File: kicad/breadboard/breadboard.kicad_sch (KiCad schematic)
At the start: 11 parts, among them U1 74LS245, U2 74LS245, U3 UPdruino_v3.0, U4 74LS245, U5 74LS245

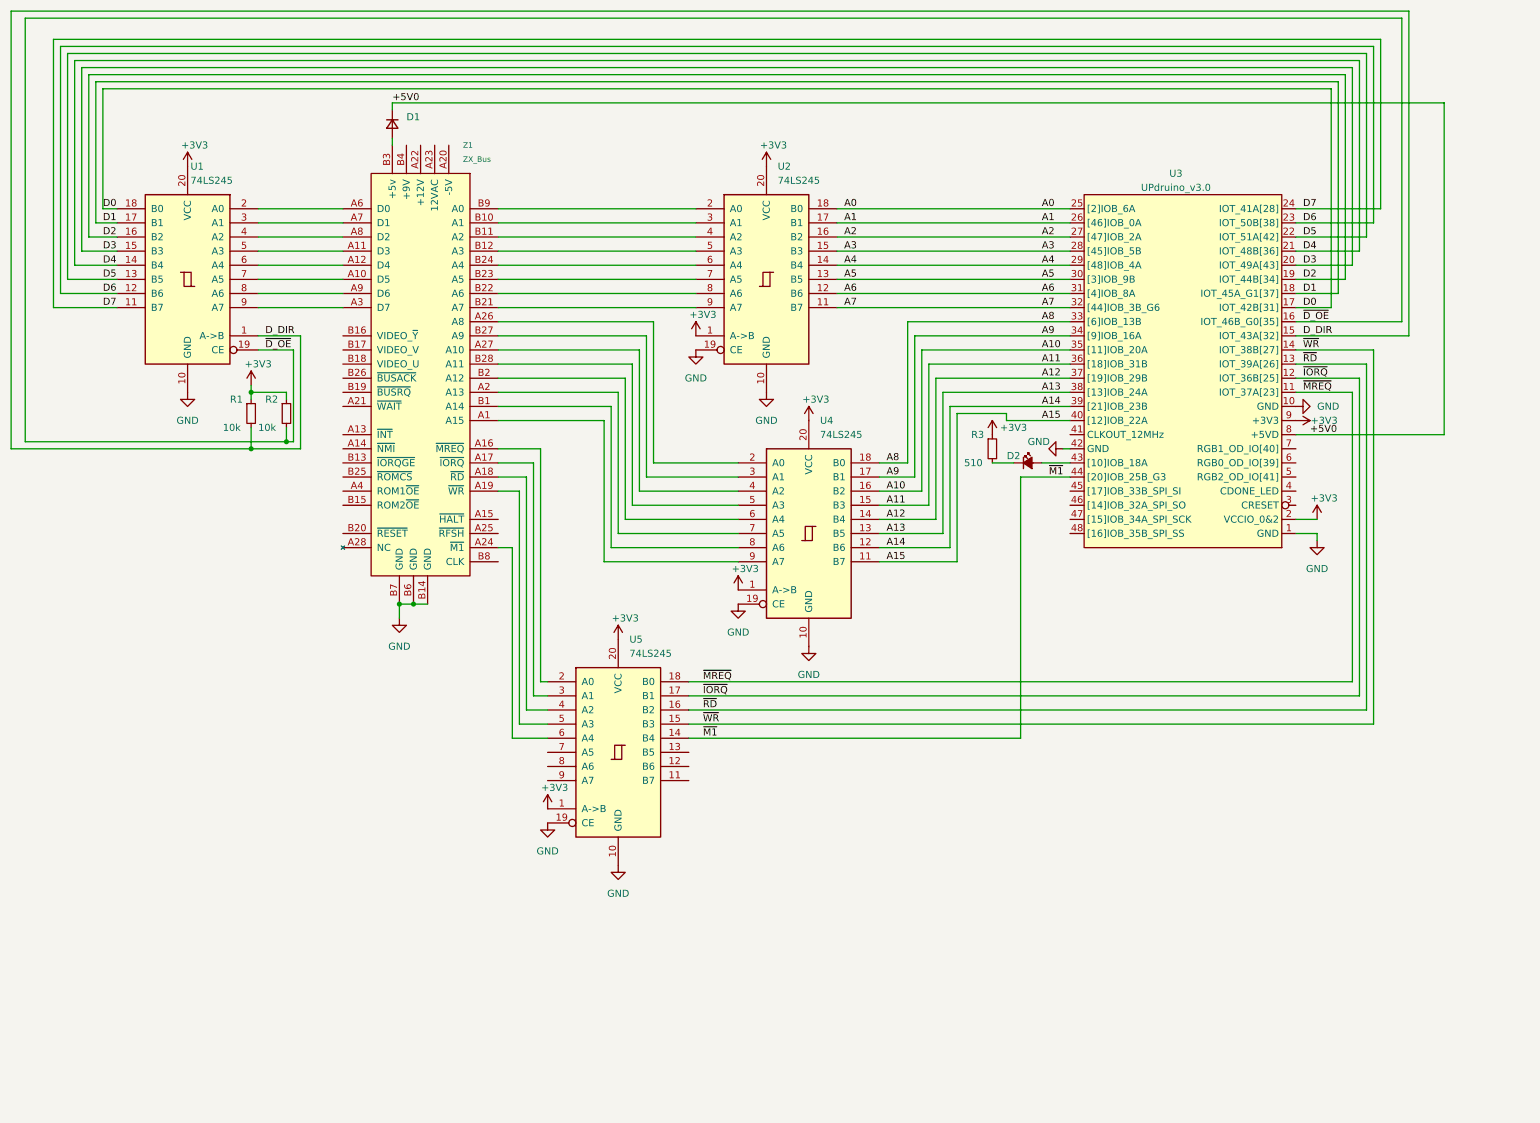
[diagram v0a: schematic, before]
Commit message: schematics: update breadboard: add Raspberry PI Zero and Spectrum ROMCS signal;
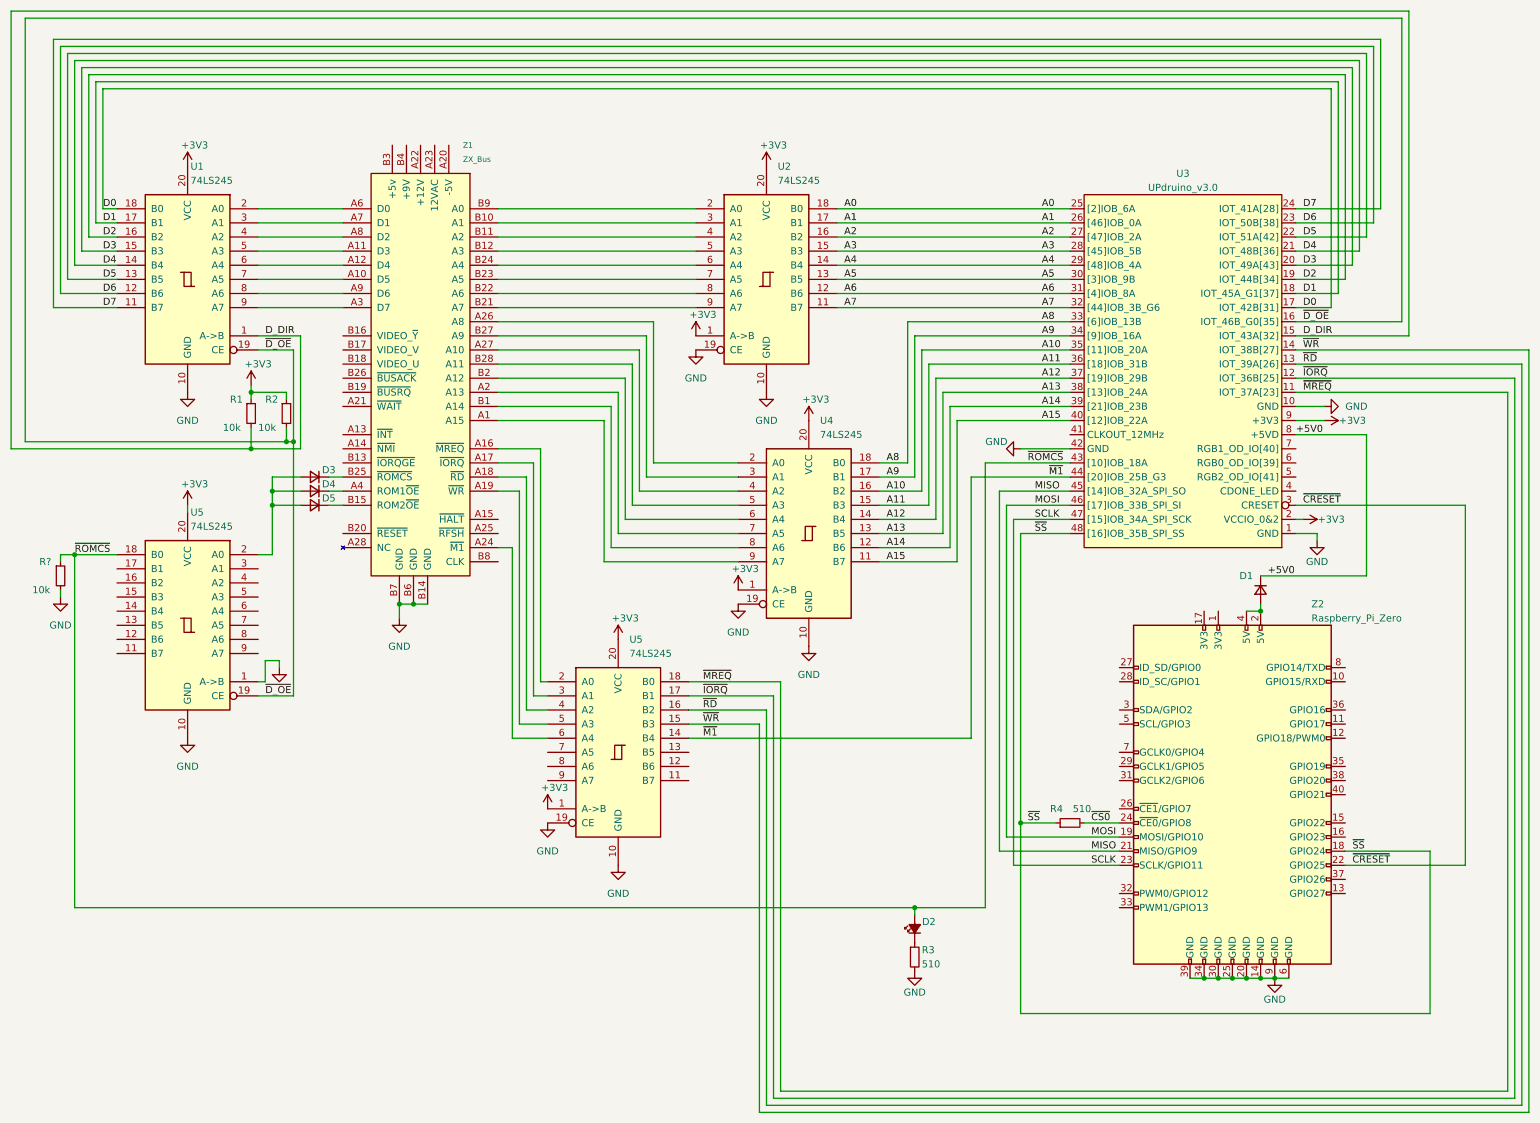
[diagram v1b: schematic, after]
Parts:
- added D3, D4, D5: D_Small, symbol Device:D_Small
- added R4: 510, symbol Device:R_Small
- added R?: 10k, symbol Device:R_Small
- added U5: 74LS245, symbol 74xx:74LS245
- added Z2: Raspberry_Pi_Zero, symbol Connector:Raspberry_Pi_2_3
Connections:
- net +3V3: now also U5.20 (VCC); no longer R3.1
- net GND: now also R3.2, R?.2, U5.1 (A->B), U5.10 (GND), Z2.14 (GND), Z2.20 (GND), Z2.25 (GND), Z2.30 (GND), Z2.34 (GND), Z2.39 (GND), Z2.6 (GND), Z2.9 (GND)
- net ~{D_OE}: now also U5.19 (CE)
- net at D2.1 (K): now also R3.1; no longer R3.2
- net at D1.2 (A): now also Z2.2 (5V), Z2.4 (5V); no longer Z1.B3 (+5v)
- net at Z1.A4 (ROM1~{OE}): now also D4.1 (K)
- net at Z1.B15 (ROM2~{OE}): now also D5.1 (K)
- net at Z1.B25 (~{ROMCS}): now also D3.1 (K)
- net ~{ROMCS}: now reaches D2.2 (A), U3.43 ([10]IOB_18A)
- net ~{ROMCS}: now also R?.1, U5.18 (B0)
- net ~{CRESET}: now reaches U3.3 (CRESET)
- net ~{CRESET}: now also Z2.22 (GPIO25)
- net MISO: now reaches U3.45 ([14]IOB_32A_SPI_SO)
- net MISO: now also Z2.21 (MISO/GPIO9)
- net MOSI: now reaches U3.46 ([17]IOB_33B_SPI_SI)
- net MOSI: now also Z2.19 (MOSI/GPIO10)
- net SCLK: now reaches U3.47 ([15]IOB_34A_SPI_SCK)
- net SCLK: now also Z2.23 (SCLK/GPIO11)
- net ~{SS}: now reaches U3.48 ([16]IOB_35B_SPI_SS)
- net ~{SS}: now also R4.1, Z2.18 (GPIO24)
- new net: D3.2 (A), D4.2 (A), D5.2 (A), U5.2 (A0)
- new net ~{CS0}: R4.2, Z2.24 (~{CE0}/GPIO8)
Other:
- moved on the sheet: D2, R3
